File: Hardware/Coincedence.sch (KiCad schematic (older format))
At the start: 10 parts

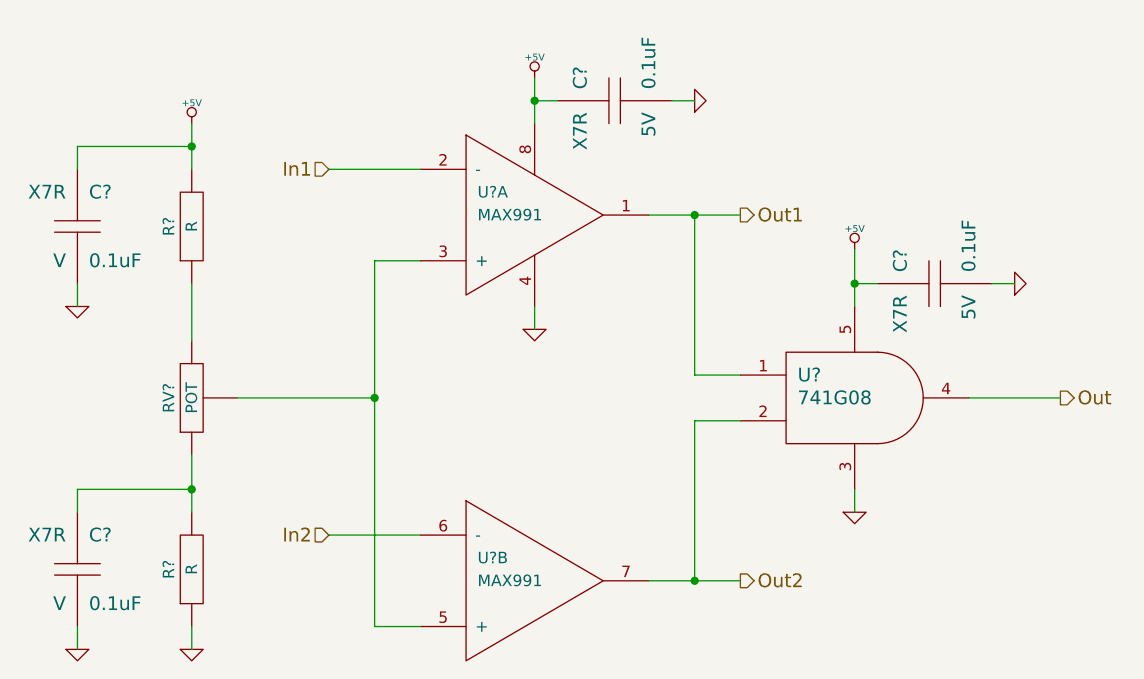
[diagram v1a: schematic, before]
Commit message: Fill BOM fields for coincidence section
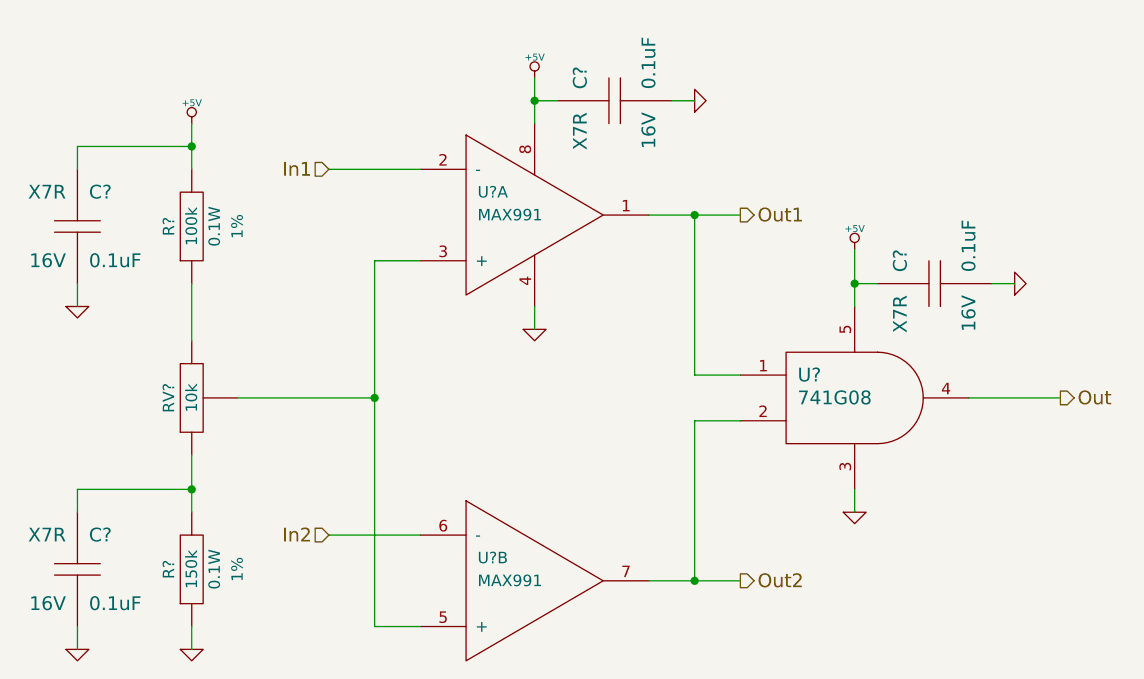
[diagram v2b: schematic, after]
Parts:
- removed C? (x4): 0.1uF, ~, symbol C
- added C? (x4): 0.1uF, CAPC1608, symbol C
- R?: value R -> 150k; footprint ~ -> RESC1608; Distributor Part No (none) -> 311-150KHRCT-ND; MFR Name (none) -> Yageo; MFR Part No (none) -> RC0603FR-07150KL; Power W -> 0.1W; Tolerance % -> 1%
- R?: value R -> 100k; footprint ~ -> RESC1608; Distributor Part No (none) -> 311-100KHRCT-ND; MFR Name (none) -> Yageo; MFR Part No (none) -> RC0603FR-07100KL; Power W -> 0.1W; Tolerance % -> 1%
- RV?: value POT -> 10k; footprint ~ -> POT-3361P; Distributor Part No (none) -> 3361P-103GLFCT-ND; MFR Name (none) -> Bourns; MFR Part No (none) -> 3361P-1-103GLF; Power W -> 0.5W; Tolerance % -> 10%
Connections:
- net +5V: now also C?.1, C?.1, C?.1
- net GND: now also C?.2, C?.2, C?.2, C?.2
- net at R?.2, RV?.1: now also C?.1
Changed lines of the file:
@@
-$EndComp
-$Comp
-L C C?
-U 1 1 523F903F
-P 3750 2800
-F 0 "C?" H 3800 2950 60  0000 L CNN
-F 1 "0.1uF" H 3800 2650 60  0000 L CNN
-F 2 "~" H 3750 2800 60  0000 C CNN
-F 3 "~" H 3750 2800 60  0000 C CNN
-F 4 "5V" H 3700 2650 60  0000 R CNN "Voltage"
-F 5 "X7R" H 3700 2950 60  0000 R CNN "Dielectric"
-	1    3750 2800
-	0    -1   -1   0
 $EndComp
 $Comp
@@
 P 1900 4100
 F 0 "RV?" H 1900 4200 50  0000 C CNN
-F 1 "POT" H 1900 4100 50  0000 C CNN
-F 2 "~" H 1900 4100 60  0000 C CNN
+F 1 "10k" H 1900 4100 50  0000 C CNN
+F 2 "POT-3361P" H 1900 4100 60  0001 C CNN
 F 3 "~" H 1900 4100 60  0000 C CNN
-F 4 "W" H 1950 4000 50  0001 L CNN "Power"
-F 5 "%" H 1850 4000 50  0001 R CNN "Tolerance"
+F 4 "Bourns" H 1900 4100 60  0001 C CNN "MFR Name"
+F 5 "3361P-1-103GLF" H 1900 4100 60  0001 C CNN "MFR Part No"
+F 6 "3361P-103GLFCT-ND" H 1900 4100 60  0001 C CNN "Distributor Part No"
+F 7 "0.5W" H 1950 4000 50  0001 L CNN "Power"
+F 8 "10%" H 1850 4000 50  0001 R CNN "Tolerance"
 	1    1900 4100
 	0    -1   -1   0
@@
 P 1900 4850
 F 0 "R?" H 1900 4950 50  0000 C CNN
-F 1 "R" H 1900 4850 50  0000 C CNN
-F 2 "~" H 1900 4850 60  0000 C CNN
+F 1 "150k" H 1900 4850 50  0000 C CNN
+F 2 "RESC1608" H 1900 4850 60  0001 C CNN
 F 3 "~" H 1900 4850 60  0000 C CNN
-F 4 "W" H 1900 4750 50  0001 C CNN "Power"
-F 5 "%" H 1900 4650 50  0001 C CNN "Tolerance"
+F 4 "Yageo" H 1900 4850 60  0001 C CNN "MFR Name"
+F 5 "RC0603FR-07150KL" H 1900 4850 60  0001 C CNN "MFR Part No"
+F 6 "311-150KHRCT-ND" H 1900 4850 60  0001 C CNN "Distributor Part No"
+F 7 "0.1W" H 1900 4750 50  0000 C CNN "Power"
+F 8 "1%" H 1900 4650 50  0000 C CNN "Tolerance"
 	1    1900 4850
 	0    -1   -1   0
@@
 P 1900 3350
 F 0 "R?" H 1900 3450 50  0000 C CNN
-F 1 "R" H 1900 3350 50  0000 C CNN
-F 2 "~" H 1900 3350 60  0000 C CNN
+F 1 "100k" H 1900 3350 50  0000 C CNN
+F 2 "RESC1608" H 1900 3350 60  0001 C CNN
 F 3 "~" H 1900 3350 60  0000 C CNN
-F 4 "W" H 1900 3250 50  0001 C CNN "Power"
-F 5 "%" H 1900 3150 50  0001 C CNN "Tolerance"
+F 4 "Yageo" H 1900 3350 60  0001 C CNN "MFR Name"
+F 5 "RC0603FR-07100KL" H 1900 3350 60  0001 C CNN "MFR Part No"
+F 6 "311-100KHRCT-ND" H 1900 3350 60  0001 C CNN "Distributor Part No"
+F 7 "0.1W" H 1900 3250 50  0000 C CNN "Power"
+F 8 "1%" H 1900 3150 50  0000 C CNN "Tolerance"
 	1    1900 3350
 	0    -1   -1   0
-$EndComp
-$Comp
-L C C?
-U 1 1 523FBDE1
-P 1400 4850
-F 0 "C?" H 1450 5000 60  0000 L CNN
-F 1 "0.1uF" H 1450 4700 60  0000 L CNN
-F 2 "~" H 1400 4850 60  0000 C CNN
-F 3 "~" H 1400 4850 60  0000 C CNN
-F 4 "V" H 1350 4700 60  0000 R CNN "Voltage"
-F 5 "X7R" H 1350 5000 60  0000 R CNN "Dielectric"
-	1    1400 4850
-	1    0    0    -1
-$EndComp
-$Comp
-L C C?
-U 1 1 523FBE4F
-P 1400 3350
-F 0 "C?" H 1450 3500 60  0000 L CNN
-F 1 "0.1uF" H 1450 3200 60  0000 L CNN
-F 2 "~" H 1400 3350 60  0000 C CNN
-F 3 "~" H 1400 3350 60  0000 C CNN
-F 4 "V" H 1350 3200 60  0000 R CNN "Voltage"
-F 5 "X7R" H 1350 3500 60  0000 R CNN "Dielectric"
-	1    1400 3350
-	1    0    0    -1
 $EndComp
 $Comp
@@
 Connection ~ 4100 4900
 $Comp
-L C C?
-U 1 1 523FC3EB
-P 5150 3600
-F 0 "C?" H 5200 3750 60  0000 L CNN
-F 1 "0.1uF" H 5200 3450 60  0000 L CNN
-F 2 "~" H 5150 3600 60  0000 C CNN
-F 3 "~" H 5150 3600 60  0000 C CNN
-F 4 "5V" H 5100 3450 60  0000 R CNN "Voltage"
-F 5 "X7R" H 5100 3750 60  0000 R CNN "Dielectric"
-	1    5150 3600
-	0    -1   -1   0
-$EndComp
-$Comp
 L +5V #PWR?
 U 1 1 523FC3F3
@@
 	1    0    0    -1
 $EndComp
+$Comp
+L C C?
+U 1 1 52412F31
+P 3750 2800
+F 0 "C?" H 3800 2950 60  0000 L CNN
+F 1 "0.1uF" H 3800 2650 60  0000 L CNN
+F 2 "CAPC1608" H 3750 2800 60  0001 C CNN
+F 3 "~" H 3750 2800 60  0000 C CNN
+F 4 "Samsung" H 3750 2800 60  0001 C CNN "MFR Name"
+F 5 "CL10B104KO8NNNC" H 3750 2800 60  0001 C CNN "MFR Part No"
+F 6 "1276-1005-1-ND" H 3750 2800 60  0001 C CNN "Distributor Part No"
+F 7 "16V" H 3700 2650 60  0000 R CNN "Voltage"
+F 8 "X7R" H 3700 2950 60  0000 R CNN "Dielectric"
+	1    3750 2800
+	0    -1   -1   0
+$EndComp
+$Comp
+L C C?
+U 1 1 52412F50
+P 5150 3600
+F 0 "C?" H 5200 3750 60  0000 L CNN
+F 1 "0.1uF" H 5200 3450 60  0000 L CNN
+F 2 "CAPC1608" H 5150 3600 60  0001 C CNN
+F 3 "~" H 5150 3600 60  0000 C CNN
+F 4 "Samsung" H 5150 3600 60  0001 C CNN "MFR Name"
+F 5 "CL10B104KO8NNNC" H 5150 3600 60  0001 C CNN "MFR Part No"
+F 6 "1276-1005-1-ND" H 5150 3600 60  0001 C CNN "Distributor Part No"
+F 7 "16V" H 5100 3450 60  0000 R CNN "Voltage"
+F 8 "X7R" H 5100 3750 60  0000 R CNN "Dielectric"
+	1    5150 3600
+	0    -1   -1   0
+$EndComp
+$Comp
+L C C?
+U 1 1 52412F5B
+P 1400 3350
+F 0 "C?" H 1450 3500 60  0000 L CNN
+F 1 "0.1uF" H 1450 3200 60  0000 L CNN
+F 2 "CAPC1608" H 1400 3350 60  0001 C CNN
+F 3 "~" H 1400 3350 60  0000 C CNN
+F 4 "Samsung" H 1400 3350 60  0001 C CNN "MFR Name"
+F 5 "CL10B104KO8NNNC" H 1400 3350 60  0001 C CNN "MFR Part No"
+F 6 "1276-1005-1-ND" H 1400 3350 60  0001 C CNN "Distributor Part No"
+F 7 "16V" H 1350 3200 60  0000 R CNN "Voltage"
+F 8 "X7R" H 1350 3500 60  0000 R CNN "Dielectric"
+	1    1400 3350
+	1    0    0    -1
+$EndComp
+$Comp
+L C C?
+U 1 1 52412F66
+P 1400 4850
+F 0 "C?" H 1450 5000 60  0000 L CNN
+F 1 "0.1uF" H 1450 4700 60  0000 L CNN
+F 2 "CAPC1608" H 1400 4850 60  0001 C CNN
+F 3 "~" H 1400 4850 60  0000 C CNN
+F 4 "Samsung" H 1400 4850 60  0001 C CNN "MFR Name"
+F 5 "CL10B104KO8NNNC" H 1400 4850 60  0001 C CNN "MFR Part No"
+F 6 "1276-1005-1-ND" H 1400 4850 60  0001 C CNN "Distributor Part No"
+F 7 "16V" H 1350 4700 60  0000 R CNN "Voltage"
+F 8 "X7R" H 1350 5000 60  0000 R CNN "Dielectric"
+	1    1400 4850
+	1    0    0    -1
+$EndComp

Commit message: Initial annotation
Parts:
- gave numbers to parts that had none: 9
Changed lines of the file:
@@
 Out
 $Comp
-L OPAMP-DUAL U?
+L OPAMP-DUAL U3
 U 1 1 523F8EB0
 P 3400 3300
-F 0 "U?" H 3150 3400 50  0000 L CNN
+F 0 "U3" H 3150 3400 50  0000 L CNN
 F 1 "MAX991" H 3150 3300 50  0000 L CNN
 F 2 "~" H 3400 3300 60  0000 C CNN
@@
 $EndComp
 $Comp
-L +5V #PWR?
+L +5V #PWR21
 U 1 1 523F90E7
 P 3400 2700
-F 0 "#PWR?" H 3400 2790 20  0001 C CNN
+F 0 "#PWR21" H 3400 2790 20  0001 C CNN
 F 1 "+5V" H 3400 2790 30  0000 C CNN
 F 2 "" H 3400 2700 60  0000 C CNN
@@
 Connection ~ 3400 2800
 $Comp
-L GND #PWR?
+L GND #PWR22
 U 1 1 523F9103
 P 4100 2800
-F 0 "#PWR?" H 4100 2800 30  0001 C CNN
+F 0 "#PWR22" H 4100 2800 30  0001 C CNN
 F 1 "GND" H 4100 2730 30  0001 C CNN
 F 2 "" H 4100 2800 60  0000 C CNN
@@
 $EndComp
 $Comp
-L GND #PWR?
+L GND #PWR27
 U 1 1 523F9112
 P 3400 3800
-F 0 "#PWR?" H 3400 3800 30  0001 C CNN
+F 0 "#PWR27" H 3400 3800 30  0001 C CNN
 F 1 "GND" H 3400 3730 30  0001 C CNN
 F 2 "" H 3400 3800 60  0000 C CNN
@@
 	3900 4900 4300 4900
 $Comp
-L POT RV?
+L POT RV1
 U 1 1 523FBD66
 P 1900 4100
-F 0 "RV?" H 1900 4200 50  0000 C CNN
+F 0 "RV1" H 1900 4200 50  0000 C CNN
 F 1 "10k" H 1900 4100 50  0000 C CNN
 F 2 "POT-3361P" H 1900 4100 60  0001 C CNN
@@
 $EndComp
 $Comp
-L R R?
+L R R11
 U 1 1 523FBD81
 P 1900 4850
-F 0 "R?" H 1900 4950 50  0000 C CNN
+F 0 "R11" H 1900 4950 50  0000 C CNN
 F 1 "150k" H 1900 4850 50  0000 C CNN
 F 2 "RESC1608" H 1900 4850 60  0001 C CNN
@@
 $EndComp
 $Comp
-L R R?
+L R R10
 U 1 1 523FBDC6
 P 1900 3350
-F 0 "R?" H 1900 3450 50  0000 C CNN
+F 0 "R10" H 1900 3450 50  0000 C CNN
 F 1 "100k" H 1900 3350 50  0000 C CNN
 F 2 "RESC1608" H 1900 3350 60  0001 C CNN
@@
 $EndComp
 $Comp
-L +5V #PWR?
+L +5V #PWR23
 U 1 1 523FBE57
 P 1900 2900
-F 0 "#PWR?" H 1900 2990 20  0001 C CNN
+F 0 "#PWR23" H 1900 2990 20  0001 C CNN
 F 1 "+5V" H 1900 2990 30  0000 C CNN
 F 2 "" H 1900 2900 60  0000 C CNN
@@
 Connection ~ 1900 4500
 $Comp
-L GND #PWR?
+L GND #PWR29
 U 1 1 523FBEA8
 P 1400 5200
-F 0 "#PWR?" H 1400 5200 30  0001 C CNN
+F 0 "#PWR29" H 1400 5200 30  0001 C CNN
 F 1 "GND" H 1400 5130 30  0001 C CNN
 F 2 "" H 1400 5200 60  0000 C CNN
@@
 $EndComp
 $Comp
-L GND #PWR?
+L GND #PWR26
 U 1 1 523FBEB7
 P 1400 3700
-F 0 "#PWR?" H 1400 3700 30  0001 C CNN
+F 0 "#PWR26" H 1400 3700 30  0001 C CNN
 F 1 "GND" H 1400 3630 30  0001 C CNN
 F 2 "" H 1400 3700 60  0000 C CNN
@@
 $EndComp
 $Comp
-L GND #PWR?
+L GND #PWR30
 U 1 1 523FBEC6
 P 1900 5200
-F 0 "#PWR?" H 1900 5200 30  0001 C CNN
+F 0 "#PWR30" H 1900 5200 30  0001 C CNN
 F 1 "GND" H 1900 5130 30  0001 C CNN
 F 2 "" H 1900 5200 60  0000 C CNN
@@
 	2500 4700 2900 4700
 $Comp
-L GATE-AND U?
+L GATE-AND U4
 U 1 1 523FC36F
 P 4800 4100
-F 0 "U?" H 4550 4200 60  0000 L CNN
+F 0 "U4" H 4550 4200 60  0000 L CNN
 F 1 "741G08" H 4550 4100 60  0000 L CNN
 F 2 "" H 4800 4100 60  0000 C CNN
@@
 Connection ~ 4100 4900
 $Comp
-L +5V #PWR?
+L +5V #PWR24
 U 1 1 523FC3F3
 P 4800 3450
-F 0 "#PWR?" H 4800 3540 20  0001 C CNN
+F 0 "#PWR24" H 4800 3540 20  0001 C CNN
 F 1 "+5V" H 4800 3540 30  0000 C CNN
 F 2 "" H 4800 3450 60  0000 C CNN
@@
 Connection ~ 4800 3600
 $Comp
-L GND #PWR?
+L GND #PWR28
 U 1 1 523FC44B
 P 4800 4600
-F 0 "#PWR?" H 4800 4600 30  0001 C CNN
+F 0 "#PWR28" H 4800 4600 30  0001 C CNN
 F 1 "GND" H 4800 4530 30  0001 C CNN
 F 2 "" H 4800 4600 60  0000 C CNN
@@
 	5700 4100 5300 4100
 $Comp
-L GND #PWR?
+L GND #PWR25
 U 1 1 523FC558
 P 5500 3600
-F 0 "#PWR?" H 5500 3600 30  0001 C CNN
+F 0 "#PWR25" H 5500 3600 30  0001 C CNN
 F 1 "GND" H 5500 3530 30  0001 C CNN
 F 2 "" H 5500 3600 60  0000 C CNN
@@
 	5500 3600 5400 3600
 $Comp
-L OPAMP-DUAL U?
+L OPAMP-DUAL U3
 U 2 1 523FC67F
 P 3400 4900
-F 0 "U?" H 3150 5000 50  0000 L CNN
+F 0 "U3" H 3150 5000 50  0000 L CNN
 F 1 "MAX991" H 3150 4900 50  0000 L CNN
 F 2 "~" H 3400 4900 60  0000 C CNN
@@
 $EndComp
 $Comp
-L C C?
+L C C12
 U 1 1 52412F31
 P 3750 2800
-F 0 "C?" H 3800 2950 60  0000 L CNN
+F 0 "C12" H 3800 2950 60  0000 L CNN
 F 1 "0.1uF" H 3800 2650 60  0000 L CNN
 F 2 "CAPC1608" H 3750 2800 60  0001 C CNN
@@
 $EndComp
 $Comp
-L C C?
+L C C14
 U 1 1 52412F50
 P 5150 3600
-F 0 "C?" H 5200 3750 60  0000 L CNN
+F 0 "C14" H 5200 3750 60  0000 L CNN
 F 1 "0.1uF" H 5200 3450 60  0000 L CNN
 F 2 "CAPC1608" H 5150 3600 60  0001 C CNN
@@
 $EndComp
 $Comp
-L C C?
+L C C13
 U 1 1 52412F5B
 P 1400 3350
-F 0 "C?" H 1450 3500 60  0000 L CNN
+F 0 "C13" H 1450 3500 60  0000 L CNN
 F 1 "0.1uF" H 1450 3200 60  0000 L CNN
 F 2 "CAPC1608" H 1400 3350 60  0001 C CNN
@@
 $EndComp
 $Comp
-L C C?
+L C C15
 U 1 1 52412F66
 P 1400 4850
-F 0 "C?" H 1450 5000 60  0000 L CNN
+F 0 "C15" H 1450 5000 60  0000 L CNN
 F 1 "0.1uF" H 1450 4700 60  0000 L CNN
 F 2 "CAPC1608" H 1400 4850 60  0001 C CNN
